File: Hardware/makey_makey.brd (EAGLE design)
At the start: 94 x 48.3 mm, 73 parts, among them U1 ATMEGA32U4TQFP, X1 USBSMD, Y1 16MHz

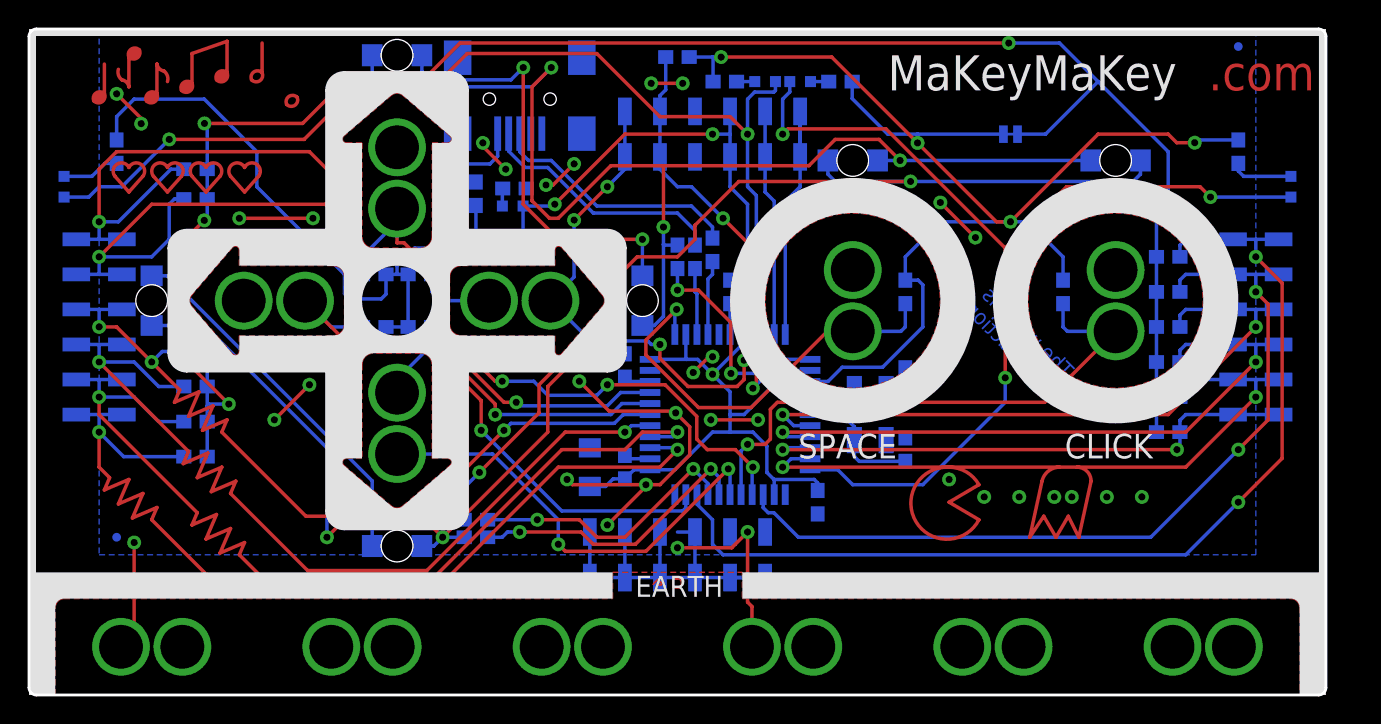
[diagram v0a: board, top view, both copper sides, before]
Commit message: Updated board layout.
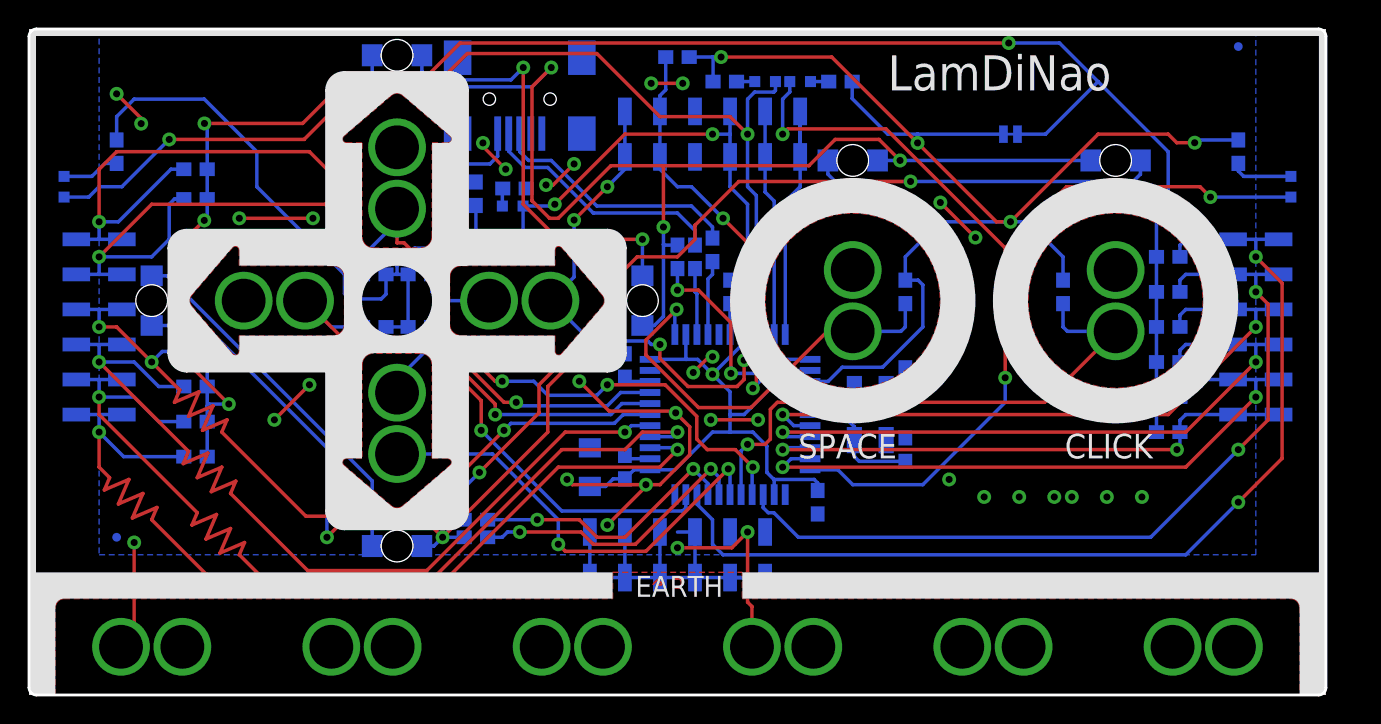
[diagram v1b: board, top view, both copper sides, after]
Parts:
- removed JP9: LOGO-SFENEW, SparkFun:SFE-NEW-WEBLOGO
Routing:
- net D1: track 78.5 -> 48.1 mm
- net N$43: track 18.5 -> 0.00 mm
- net N$54: track 9.15 -> 0.00 mm
- net N$37: track 8.77 -> 0.00 mm
- net N$42: track 7.63 -> 0.00 mm
- net N$32: track 5.45 -> 0.00 mm
- net N$35: track 5.45 -> 0.00 mm
- net N$34: track 5.45 -> 0.00 mm
- net N$33: track 5.45 -> 0.00 mm
- net N$20: track 3.99 -> 0.00 mm
- net N$19: track 1.83 -> 0.00 mm
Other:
- board text added: "Based on Makey Makey"
- board text added: "FABLAB SAIGON"
- board text added: "LamDiNao"
- board text added: "PAPCODIENTU"
- board text removed: ".com"
- board text removed: "MaKeyMaKey"
- board text removed: "The world is"
- board text removed: "a construction kit"
